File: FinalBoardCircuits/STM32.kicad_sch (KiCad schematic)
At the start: 23 parts, among them J4 SWD, SW1 SW_SPDT, U4 STM32F405RGT6, Y1 16MHz

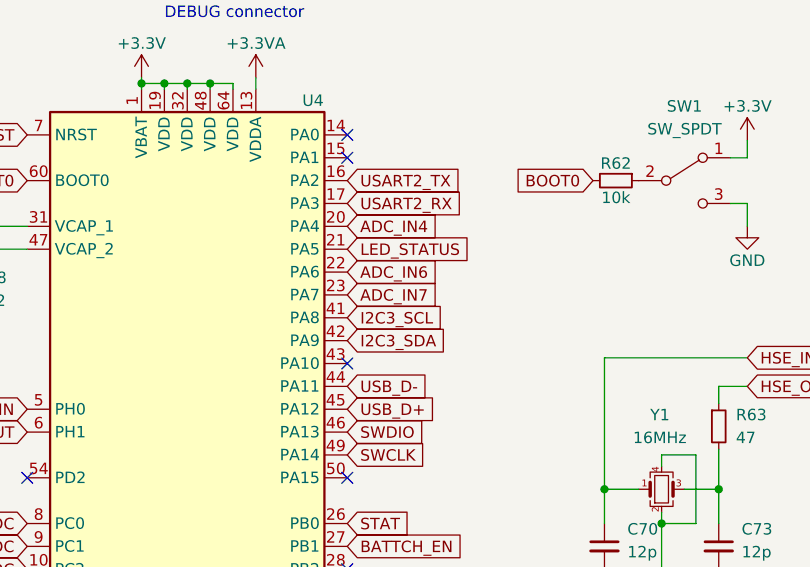
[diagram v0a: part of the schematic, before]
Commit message: Added fuel guage
Added fuel guage circuit to the final design.
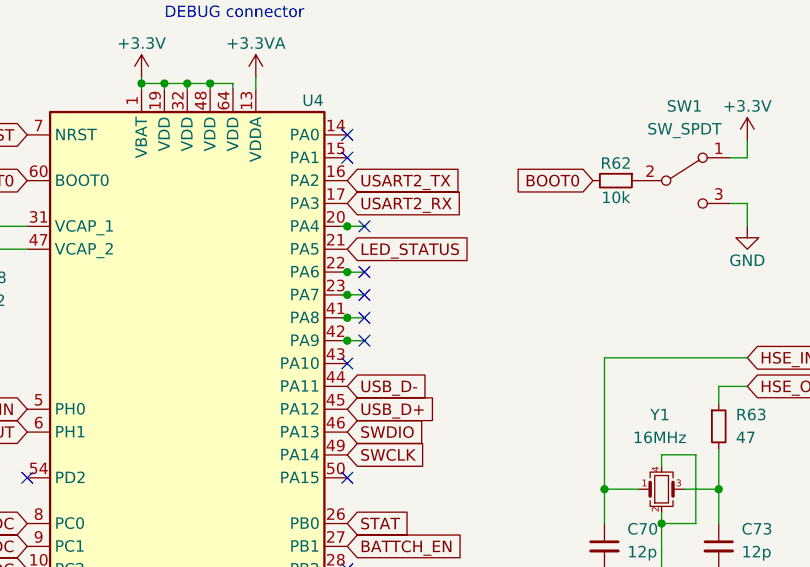
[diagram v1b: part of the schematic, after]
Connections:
- net ADC_IN4: no longer names the net of U4.20 (PA4)
- net ADC_IN6: no longer names the net of U4.22 (PA6)
- net ADC_IN7: no longer names the net of U4.23 (PA7)
- net I2C3_SCL: no longer names the net of U4.41 (PA8)
- net I2C3_SDA: no longer names the net of U4.42 (PA9)
- no-connect marks 15 -> 20
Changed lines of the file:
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@@
   (junction (at 177.165 41.275) (diameter 0) (color 0 0 0 0)
   )
+  (junction (at 147.955 91.44) (diameter 0) (color 0 0 0 0)
+  )
   (junction (at 62.23 36.195) (diameter 0) (color 0 0 0 0)
   )
   (junction (at 189.23 107.95) (diameter 0) (color 0 0 0 0)
   )
+  (junction (at 147.955 88.9) (diameter 0) (color 0 0 0 0)
+  )
+  (junction (at 147.955 83.82) (diameter 0) (color 0 0 0 0)
+  )
   (junction (at 90.17 42.545) (diameter 0) (color 0 0 0 0)
   )
@@
   (junction (at 130.175 62.865) (diameter 0) (color 0 0 0 0)
   )
+  (junction (at 147.955 78.74) (diameter 0) (color 0 0 0 0)
+  )
   (junction (at 127.635 155.575) (diameter 0) (color 0 0 0 0)
   )
@@
   )
   (junction (at 125.73 44.45) (diameter 0) (color 0 0 0 0)
+  )
+  (junction (at 147.955 86.36) (diameter 0) (color 0 0 0 0)
   )
   (junction (at 90.17 36.195) (diameter 0) (color 0 0 0 0)
@@
   (no_connect (at 147.955 68.58))
   (no_connect (at 147.955 132.08))
+  (no_connect (at 149.86 86.36))
   (no_connect (at 147.955 116.84))
   (no_connect (at 111.76 119.38))
@@
   (no_connect (at 147.955 71.12))
   (no_connect (at 112.395 149.86))
+  (no_connect (at 149.86 78.74))
   (no_connect (at 147.955 121.92))
   (no_connect (at 147.955 106.68))
+  (no_connect (at 149.86 88.9))
+  (no_connect (at 149.86 91.44))
+  (no_connect (at 149.86 83.82))
   (wire (pts (xy 80.645 42.545) (xy 90.17 42.545))
     (stroke (width 0) (type default))
@@
     (stroke (width 0) (type default))
   )
+  (wire (pts (xy 147.955 78.74) (xy 149.86 78.74))
+    (stroke (width 0) (type default))
+  )
   (wire (pts (xy 125.73 44.45) (xy 125.73 46.355))
     (stroke (width 0) (type default))
@@
     (stroke (width 0) (type default))
   )
+  (wire (pts (xy 147.955 83.82) (xy 149.86 83.82))
+    (stroke (width 0) (type default))
+  )
   (wire (pts (xy 192.405 96.52) (xy 189.23 96.52))
     (stroke (width 0) (type default))
   )
+  (wire (pts (xy 147.955 88.9) (xy 149.86 88.9))
+    (stroke (width 0) (type default))
+  )
   (wire (pts (xy 177.165 41.275) (xy 177.165 40.64))
     (stroke (width 0) (type default))
@@
     (stroke (width 0) (type default))
   )
+  (wire (pts (xy 147.32 78.74) (xy 147.955 78.74))
+    (stroke (width 0) (type default))
+  )
   (wire (pts (xy 127.635 156.21) (xy 127.635 155.575))
     (stroke (width 0) (type default))
@@
     (stroke (width 0) (type default))
   )
+  (wire (pts (xy 147.32 86.36) (xy 147.955 86.36))
+    (stroke (width 0) (type default))
+  )
   (wire (pts (xy 132.715 62.865) (xy 135.255 62.865))
     (stroke (width 0) (type default))
@@
     (stroke (width 0) (type default))
   )
+  (wire (pts (xy 147.32 91.44) (xy 147.955 91.44))
+    (stroke (width 0) (type default))
+  )
   (wire (pts (xy 125.095 62.23) (xy 125.095 62.865))
     (stroke (width 0) (type default))
@@
     (stroke (width 0) (type default))
   )
+  (wire (pts (xy 147.955 91.44) (xy 149.86 91.44))
+    (stroke (width 0) (type default))
+  )
   (wire (pts (xy 130.175 155.575) (xy 132.715 155.575))
     (stroke (width 0) (type default))
@@
     (stroke (width 0) (type default))
   )
+  (wire (pts (xy 147.955 86.36) (xy 149.86 86.36))
+    (stroke (width 0) (type default))
+  )
   (wire (pts (xy 177.165 35.56) (xy 177.165 34.925))
     (stroke (width 0) (type default))
@@
     (stroke (width 0) (type default))
   )
+  (wire (pts (xy 147.32 83.82) (xy 147.955 83.82))
+    (stroke (width 0) (type default))
+  )
   (wire (pts (xy 127.635 39.37) (xy 125.73 39.37))
     (stroke (width 0) (type default))
@@
     (stroke (width 0) (type default))
   )
+  (wire (pts (xy 147.32 88.9) (xy 147.955 88.9))
+    (stroke (width 0) (type default))
+  )
   (wire (pts (xy 137.795 62.23) (xy 137.795 63.5))
     (stroke (width 0) (type default))
@@
     )
   )
-  (global_label "ADC_IN4" (shape input) (at 147.955 78.74 0) (fields_autoplaced)
-    (effects (font (size 1.27 1.27)) (justify left))
-    (property "Intersheetrefs" "${INTERSHEET_REFS}" (at 158.1091 78.6606 0)
-      (effects (font (size 1.27 1.27)) (justify left) hide)
-    )
-  )
   (global_label "SD_CARD_SPI2_MISO" (shape input) (at 147.955 147.32 0) (fields_autoplaced)
     (effects (font (size 1.27 1.27)) (justify left))
@@
     )
   )
-  (global_label "I2C3_SCL" (shape input) (at 147.955 88.9 0) (fields_autoplaced)
-    (effects (font (size 1.27 1.27)) (justify left))
-    (property "Intersheetrefs" "${INTERSHEET_REFS}" (at 159.1371 88.8206 0)
-      (effects (font (size 1.27 1.27)) (justify left) hide)
-    )
-  )
   (global_label "BOOST_SHDN_OBC" (shape input) (at 112.395 127 180) (fields_autoplaced)
     (effects (font (size 1.27 1.27)) (justify right))
@@
     )
   )
-  (global_label "I2C3_SDA" (shape input) (at 147.955 91.44 0) (fields_autoplaced)
-    (effects (font (size 1.27 1.27)) (justify left))
-    (property "Intersheetrefs" "${INTERSHEET_REFS}" (at 159.1976 91.3606 0)
-      (effects (font (size 1.27 1.27)) (justify left) hide)
-    )
-  )
   (global_label "3.3V_STM" (shape input) (at 41.91 55.88 270) (fields_autoplaced)
     (effects (font (size 1.27 1.27)) (justify right))
@@
     )
   )
-  (global_label "ADC_IN7" (shape input) (at 147.955 86.36 0) (fields_autoplaced)
-    (effects (font (size 1.27 1.27)) (justify left))
-    (property "Intersheetrefs" "${INTERSHEET_REFS}" (at 158.1091 86.2806 0)
-      (effects (font (size 1.27 1.27)) (justify left) hide)
-    )
-  )
   (global_label "BATTCH_EN" (shape input) (at 147.955 114.3 0) (fields_autoplaced)
     (effects (font (size 1.27 1.27)) (justify left))
@@
     )
   )
-  (global_label "ADC_IN6" (shape input) (at 147.955 83.82 0) (fields_autoplaced)
-    (effects (font (size 1.27 1.27)) (justify left))
-    (property "Intersheetrefs" "${INTERSHEET_REFS}" (at 158.1091 83.7406 0)
-      (effects (font (size 1.27 1.27)) (justify left) hide)
-    )
-  )
